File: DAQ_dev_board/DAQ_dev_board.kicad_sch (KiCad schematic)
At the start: 30 parts, among them J1 Thermocouple, J2 A0, A1, J3 GPIO1, GPIO2, J4 CS, DRDY, J5 SCLK, DIN, J6 DOUT, START, J7 RESET, PDWN, U1 ADS1158IRTCR (ADC), U2 AD8495 (TC AMP), U3 OP777ARZ (OP AMP), Y1 32.768kHz

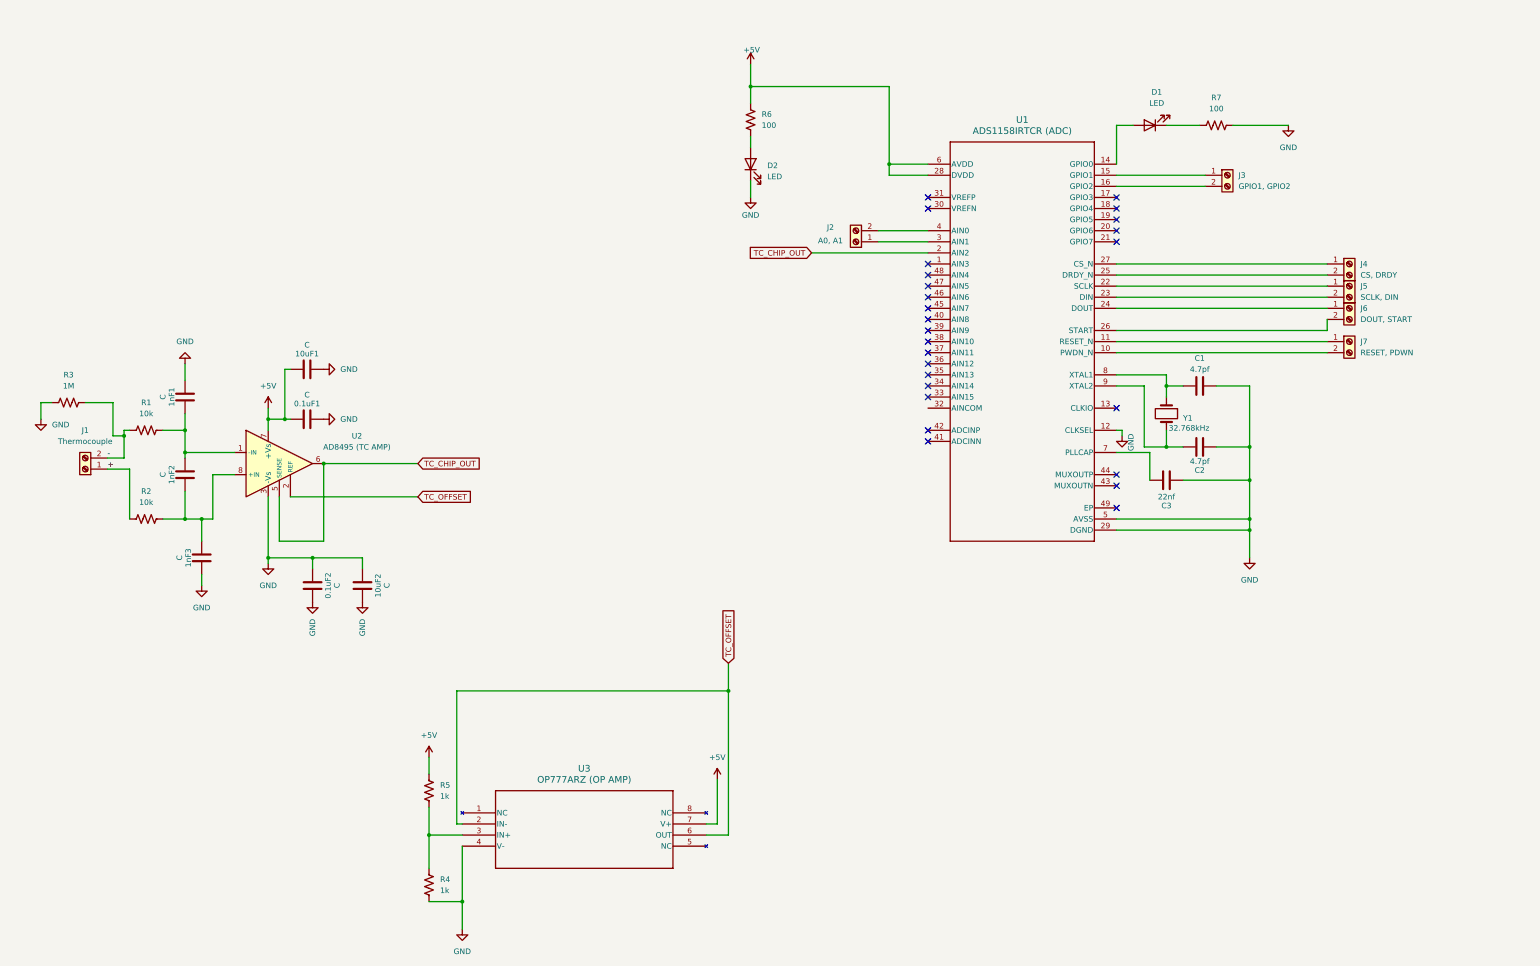
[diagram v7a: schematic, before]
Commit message: updated daq board routing
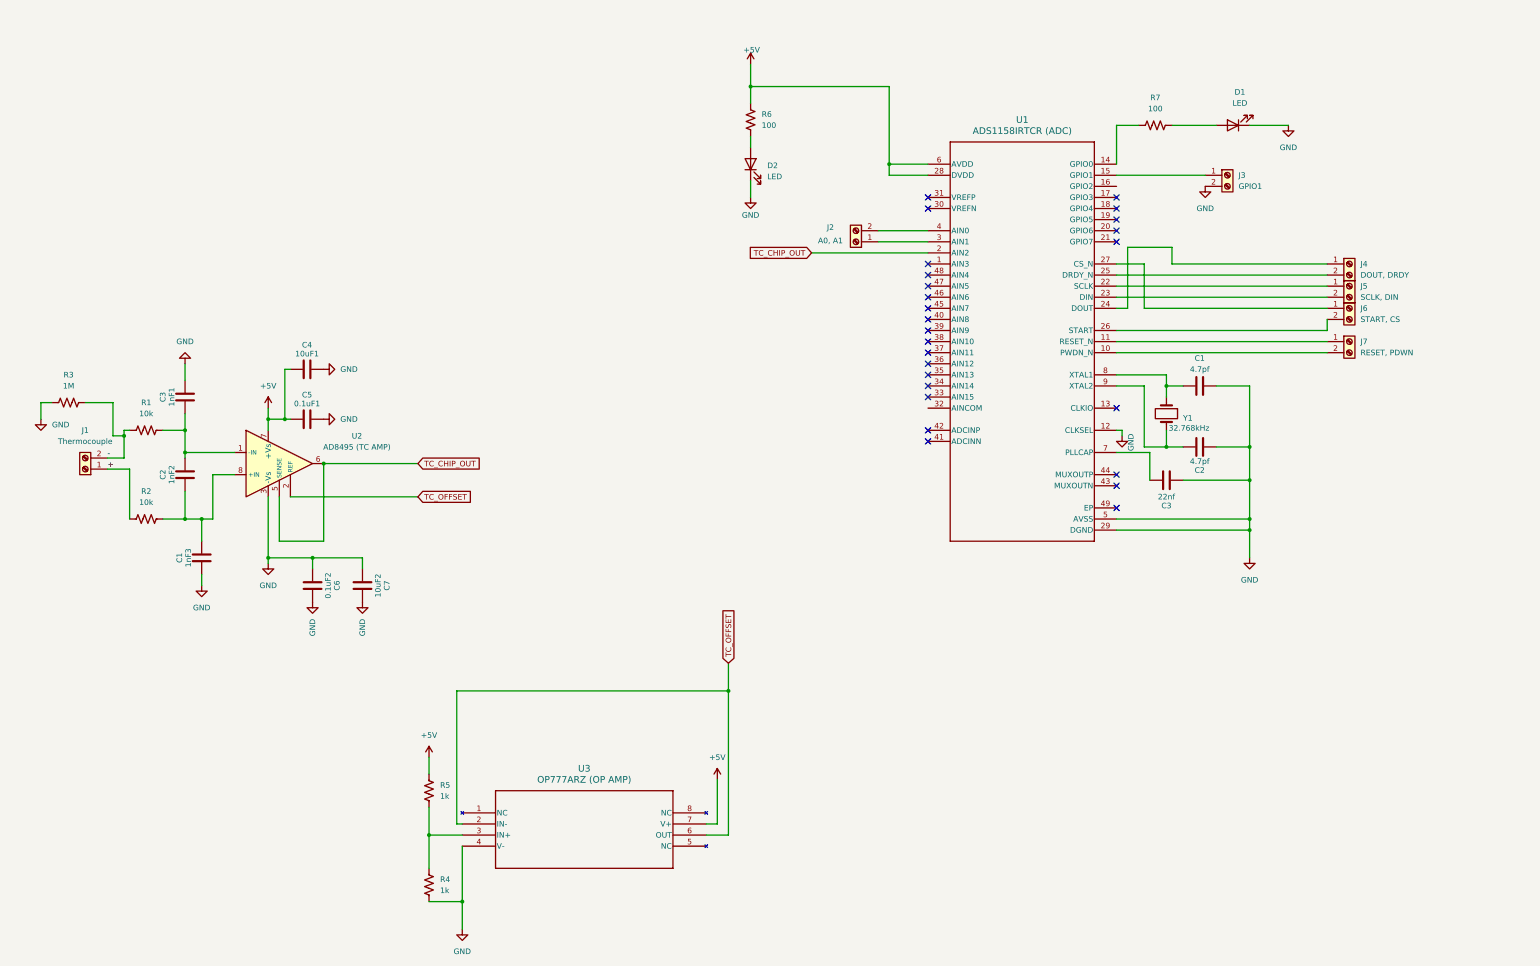
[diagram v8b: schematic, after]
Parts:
- 0.1uF1: value C -> C5
- 0.1uF2: value C -> C6
- 10uF1: value C -> C4
- 10uF2: value C -> C7
- 1nF1: value C -> C3
- 1nF2: value C -> C2
- 1nF3: value C -> C1
- J1: footprint (none) -> TerminalBlock:TerminalBlock_Xinya_XY308-2.54-2P_1x02_P2.54mm_Horizontal
- J2, J5, J7: footprint Connector_PinHeader_2.54mm:PinHeader_1x01_P2.54mm_Vertical -> TerminalBlock:TerminalBlock_Xinya_XY308-2.54-2P_1x02_P2.54mm_Horizontal
- J3: value GPIO1, GPIO2 -> GPIO1; footprint Connector_PinHeader_2.54mm:PinHeader_1x01_P2.54mm_Vertical -> TerminalBlock:TerminalBlock_Xinya_XY308-2.54-2P_1x02_P2.54mm_Horizontal
- J4: value CS, DRDY -> DOUT, DRDY; footprint Connector_PinHeader_2.54mm:PinHeader_1x01_P2.54mm_Vertical -> TerminalBlock:TerminalBlock_Xinya_XY308-2.54-2P_1x02_P2.54mm_Horizontal
- J6: value DOUT, START -> START, CS; footprint Connector_PinHeader_2.54mm:PinHeader_1x01_P2.54mm_Vertical -> TerminalBlock:TerminalBlock_Xinya_XY308-2.54-2P_1x02_P2.54mm_Horizontal
- U1: footprint RTC0048A-IPC_A -> ul_ADS1158IRTCR:RTC0048A-IPC_A
- U3: footprint R_8_ADI -> ul_ADS1158IRTCR:R_8_ADI
- Y1: footprint (none) -> ul_ADS1158IRTCR:XTAL_ABS25-32.768KHZ-6-1-T
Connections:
- net GND: now also D1.1 (K), J3.2 (Pin_2); no longer R7.2
- net at R7.1: now also U1.14 (GPIO0); no longer D1.1 (K)
- net at D1.2 (A): now also R7.2; no longer U1.14 (GPIO0)
- net at U1.16 (GPIO2): no longer J3.2 (Pin_2)
- net at U1.24 (DOUT): now also J4.1 (Pin_1); no longer J6.1 (Pin_1)
- net at U1.27 (CS_N): now also J6.1 (Pin_1); no longer J4.1 (Pin_1)
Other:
- moved on the sheet: D1, R7
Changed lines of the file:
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@@
 	(wire
 		(pts
-			(xy 287.02 48.26) (xy 294.64 48.26)
+			(xy 287.02 110.49) (xy 287.02 107.95)
 		)
 		(stroke
@@
 	(wire
 		(pts
-			(xy 287.02 110.49) (xy 287.02 107.95)
+			(xy 62.23 102.87) (xy 62.23 106.68)
 		)
 		(stroke
@@
 	(wire
 		(pts
-			(xy 62.23 102.87) (xy 62.23 106.68)
+			(xy 288.29 76.2) (xy 288.29 80.01)
 		)
 		(stroke
@@
 	(wire
 		(pts
-			(xy 275.59 90.17) (xy 323.85 90.17)
+			(xy 275.59 48.26) (xy 280.67 48.26)
 		)
 		(stroke
@@
 	(wire
 		(pts
+			(xy 288.29 80.01) (xy 323.85 80.01)
+		)
+		(stroke
+			(width 0)
+			(type default)
+		)
+	)
+	(wire
+		(pts
 			(xy 275.59 100.33) (xy 323.85 100.33)
 		)
@@
 	(wire
 		(pts
+			(xy 288.29 48.26) (xy 298.45 48.26)
+		)
+		(stroke
+			(width 0)
+			(type default)
+		)
+	)
+	(wire
+		(pts
 			(xy 298.45 107.95) (xy 306.07 107.95)
 		)
@@
 	(wire
 		(pts
-			(xy 323.85 92.71) (xy 323.85 95.25)
+			(xy 68.58 138.43) (xy 68.58 128.27)
 		)
 		(stroke
@@
 	(wire
 		(pts
-			(xy 68.58 138.43) (xy 68.58 128.27)
+			(xy 281.94 90.17) (xy 323.85 90.17)
 		)
 		(stroke
@@
 	(wire
 		(pts
-			(xy 302.26 48.26) (xy 314.96 48.26)
+			(xy 275.59 80.01) (xy 281.94 80.01)
 		)
 		(stroke
@@
 	(wire
 		(pts
-			(xy 275.59 48.26) (xy 279.4 48.26)
+			(xy 81.28 115.57) (xy 81.28 118.11)
 		)
 		(stroke
@@
 	(wire
 		(pts
-			(xy 81.28 115.57) (xy 81.28 118.11)
+			(xy 275.59 90.17) (xy 278.13 90.17)
 		)
 		(stroke
@@
 	(wire
 		(pts
-			(xy 275.59 62.23) (xy 295.91 62.23)
+			(xy 306.07 121.92) (xy 306.07 107.95)
 		)
 		(stroke
@@
 	(wire
 		(pts
-			(xy 306.07 121.92) (xy 306.07 107.95)
+			(xy 278.13 90.17) (xy 278.13 76.2)
 		)
 		(stroke
@@
 	(wire
 		(pts
+			(xy 323.85 92.71) (xy 323.85 95.25)
+		)
+		(stroke
+			(width 0)
+			(type default)
+		)
+	)
+	(wire
+		(pts
 			(xy 83.82 133.35) (xy 83.82 143.51)
 		)
@@
 	(wire
 		(pts
+			(xy 281.94 80.01) (xy 281.94 90.17)
+		)
+		(stroke
+			(width 0)
+			(type default)
+		)
+	)
+	(wire
+		(pts
 			(xy 191.77 60.96) (xy 191.77 64.77)
 		)
@@
 	(wire
 		(pts
-			(xy 118.11 193.04) (xy 118.11 196.85)
+			(xy 306.07 48.26) (xy 314.96 48.26)
 		)
 		(stroke
@@
 	(wire
 		(pts
-			(xy 276.86 119.38) (xy 276.86 118.11)
+			(xy 118.11 193.04) (xy 118.11 196.85)
 		)
 		(stroke
@@
 	(wire
 		(pts
-			(xy 275.59 80.01) (xy 323.85 80.01)
+			(xy 276.86 119.38) (xy 276.86 118.11)
 		)
 		(stroke
@@
 	(wire
 		(pts
+			(xy 278.13 76.2) (xy 288.29 76.2)
+		)
+		(stroke
+			(width 0)
+			(type default)
+		)
+	)
+	(wire
+		(pts
 			(xy 287.02 105.41) (xy 275.59 105.41)
 		)
@@
 			)
 		)
-		(property "Value" "C"
+		(property "Value" "C4"
 			(at 90.17 98.552 90)
 			(effects
@@
 			)
 		)
-		(property "Footprint" ""
+		(property "Footprint" "TerminalBlock:TerminalBlock_Xinya_XY308-2.54-2P_1x02_P2.54mm_Horizontal"
 			(at 39.37 127 0)
 			(effects
@@
 			)
 		)
-		(property "Footprint" "Connector_PinHeader_2.54mm:PinHeader_1x01_P2.54mm_Vertical"
+		(property "Footprint" "TerminalBlock:TerminalBlock_Xinya_XY308-2.54-2P_1x02_P2.54mm_Horizontal"
 			(at 215.9 74.93 0)
 			(effects
@@
 	)
 	(symbol
+		(lib_id "power:GND")
+		(at 295.91 62.23 0)
+		(unit 1)
+		(exclude_from_sim no)
+		(in_bom yes)
+		(on_board yes)
+		(dnp no)
+		(fields_autoplaced yes)
+		(property "Reference" "#PWR018"
+			(at 295.91 68.58 0)
+			(effects
+				(font
+					(size 1.27 1.27)
+				)
+				(hide yes)
+			)
+		)
+		(property "Value" "GND"
+			(at 295.91 67.31 0)
+			(effects
+				(font
+					(size 1.27 1.27)
+				)
+			)
+		)
+		(property "Footprint" ""
+			(at 295.91 62.23 0)
+			(effects
+				(font
+					(size 1.27 1.27)
+				)
+				(hide yes)
+			)
+		)
+		(property "Datasheet" ""
+			(at 295.91 62.23 0)
+			(effects
+				(font
+					(size 1.27 1.27)
+				)
+				(hide yes)
+			)
+		)
+		(property "Description" "Power symbol creates a global label with name \"GND\" , ground"
+			(at 295.91 62.23 0)
+			(effects
+				(font
+					(size 1.27 1.27)
+				)
+				(hide yes)
+			)
+		)
+		(pin "1"
+		)
+		(instances
+			(project ""
+				(path "/a39f2c3e-c1f4-493f-bbb6-b1b089f205f8"
+					(reference "#PWR018")
+					(unit 1)
+				)
+			)
+		)
+	)
+	(symbol
 		(lib_id "OP777:OP777ARZ")
 		(at 125.73 205.74 0)
@@
 			)
 		)
-		(property "Footprint" "R_8_ADI"
+		(property "Footprint" "ul_ADS1158IRTCR:R_8_ADI"
 			(at 125.73 205.74 0)
 			(effects
@@
 	(symbol
 		(lib_id "Device:LED")
-		(at 283.21 48.26 180)
+		(at 302.26 48.26 180)
 		(unit 1)
 		(exclude_from_sim no)
@@
 		(fields_autoplaced yes)
 		(property "Reference" "D1"
-			(at 284.7975 40.64 0)
+			(at 303.8475 40.64 0)
 			(effects
 				(font
@@
 		)
 		(property "Value" "LED"
-			(at 284.7975 43.18 0)
+			(at 303.8475 43.18 0)
 			(effects
 				(font
@@
 		)
 		(property "Footprint" "Capacitor_SMD:C_0603_1608Metric"
-			(at 283.21 48.26 0)
+			(at 302.26 48.26 0)
 			(effects
 				(font
@@
 		)
 		(property "Datasheet" "~"
-			(at 283.21 48.26 0)
+			(at 302.26 48.26 0)
 			(effects
 				(font
@@
 		)
 		(property "Description" "Light emitting diode"
-			(at 283.21 48.26 0)
+			(at 302.26 48.26 0)
 			(effects
 				(font
@@
 			)
 		)
-		(property "Footprint" "Connector_PinHeader_2.54mm:PinHeader_1x01_P2.54mm_Vertical"
+		(property "Footprint" "TerminalBlock:TerminalBlock_Xinya_XY308-2.54-2P_1x02_P2.54mm_Horizontal"
 			(at 328.93 97.79 0)
 			(effects
@@
 			)
 		)
-		(property "Value" "C"
+		(property "Value" "C2"
 			(at 57.15 128.27 90)
 			(effects
@@
 			)
 		)
-		(property "Footprint" "RTC0048A-IPC_A"
+		(property "Footprint" "ul_ADS1158IRTCR:RTC0048A-IPC_A"
 			(at 232.41 57.15 0)
 			(effects
@@
 			)
 		)
-		(property "Value" "DOUT, START"
+		(property "Value" "START, CS"
 			(at 331.47 92.7099 0)
 			(effects
@@
 			)
 		)
-		(property "Footprint" "Connector_PinHeader_2.54mm:PinHeader_1x01_P2.54mm_Vertical"
+		(property "Footprint" "TerminalBlock:TerminalBlock_Xinya_XY308-2.54-2P_1x02_P2.54mm_Horizontal"
 			(at 328.93 90.17 0)
 			(effects
@@
 			)
 		)
-		(property "Value" "GPIO1, GPIO2"
+		(property "Value" "GPIO1"
 			(at 303.53 62.2299 0)
 			(effects
@@
 			)
 		)
-		(property "Footprint" "Connector_PinHeader_2.54mm:PinHeader_1x01_P2.54mm_Vertical"
+		(property "Footprint" "TerminalBlock:TerminalBlock_Xinya_XY308-2.54-2P_1x02_P2.54mm_Horizontal"
 			(at 300.99 59.69 0)
 			(effects
@@
 	(symbol
 		(lib_id "Device:R_US")
-		(at 298.45 48.26 90)
+		(at 284.48 48.26 90)
 		(unit 1)
 		(exclude_from_sim no)
@@
 		(fields_autoplaced yes)
 		(property "Reference" "R7"
-			(at 298.45 41.91 90)
+			(at 284.48 41.91 90)
 			(effects
 				(font
@@
 		)
 		(property "Value" "100"
-			(at 298.45 44.45 90)
+			(at 284.48 44.45 90)
 			(effects
 				(font
@@
 		)
 		(property "Footprint" "Capacitor_SMD:C_0603_1608Metric"
-			(at 298.704 47.244 90)
+			(at 284.734 47.244 90)
 			(effects
 				(font
@@
 		)
 		(property "Datasheet" "~"
-			(at 298.45 48.26 0)
+			(at 284.48 48.26 0)
 			(effects
 				(font
@@
 		)
 		(property "Description" "Resistor, US symbol"
-			(at 298.45 48.26 0)
+			(at 284.48 48.26 0)
 			(effects
 				(font
@@
 			)
 		)
-		(property "Value" "C"
+		(property "Value" "C3"
 			(at 57.15 110.49 90)
 			(effects
@@
 			)
 		)
-		(property "Footprint" "Connector_PinHeader_2.54mm:PinHeader_1x01_P2.54mm_Vertical"
+		(property "Footprint" "TerminalBlock:TerminalBlock_Xinya_XY308-2.54-2P_1x02_P2.54mm_Horizontal"
 			(at 328.93 85.09 0)
 			(effects
@@
 			)
 		)
-		(property "Value" "C"
+		(property "Value" "C1"
 			(at 60.96 147.32 90)
 			(effects
@@
 			)
 		)
-		(property "Value" "C"
+		(property "Value" "C5"
 			(at 90.17 109.982 90)
 			(effects
@@
 			)
 		)
-		(property "Value" "C"
+		(property "Value" "C6"
 			(at 97.028 153.67 90)
 			(effects
@@
 			)
 		)
-		(property "Value" "C"
+		(property "Value" "C7"
 			(at 108.458 153.67 90)
 			(effects
@@
 			)
 		)
-		(property "Value" "CS, DRDY"
+		(property "Value" "DOUT, DRDY"
 			(at 331.47 82.5499 0)
 			(effects
@@
 			)
 		)
-		(property "Footprint" "Connector_PinHeader_2.54mm:PinHeader_1x01_P2.54mm_Vertical"
+		(property "Footprint" "TerminalBlock:TerminalBlock_Xinya_XY308-2.54-2P_1x02_P2.54mm_Horizontal"
 			(at 328.93 80.01 0)
 			(effects
@@
 			)
 		)
-		(property "Footprint" ""
+		(property "Footprint" "ul_ADS1158IRTCR:XTAL_ABS25-32.768KHZ-6-1-T"
 			(at 287.02 114.3 0)
 			(effects
